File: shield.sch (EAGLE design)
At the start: 36 parts, among them IC1 AD623R, IC2 AD623R, IC3 AD623R

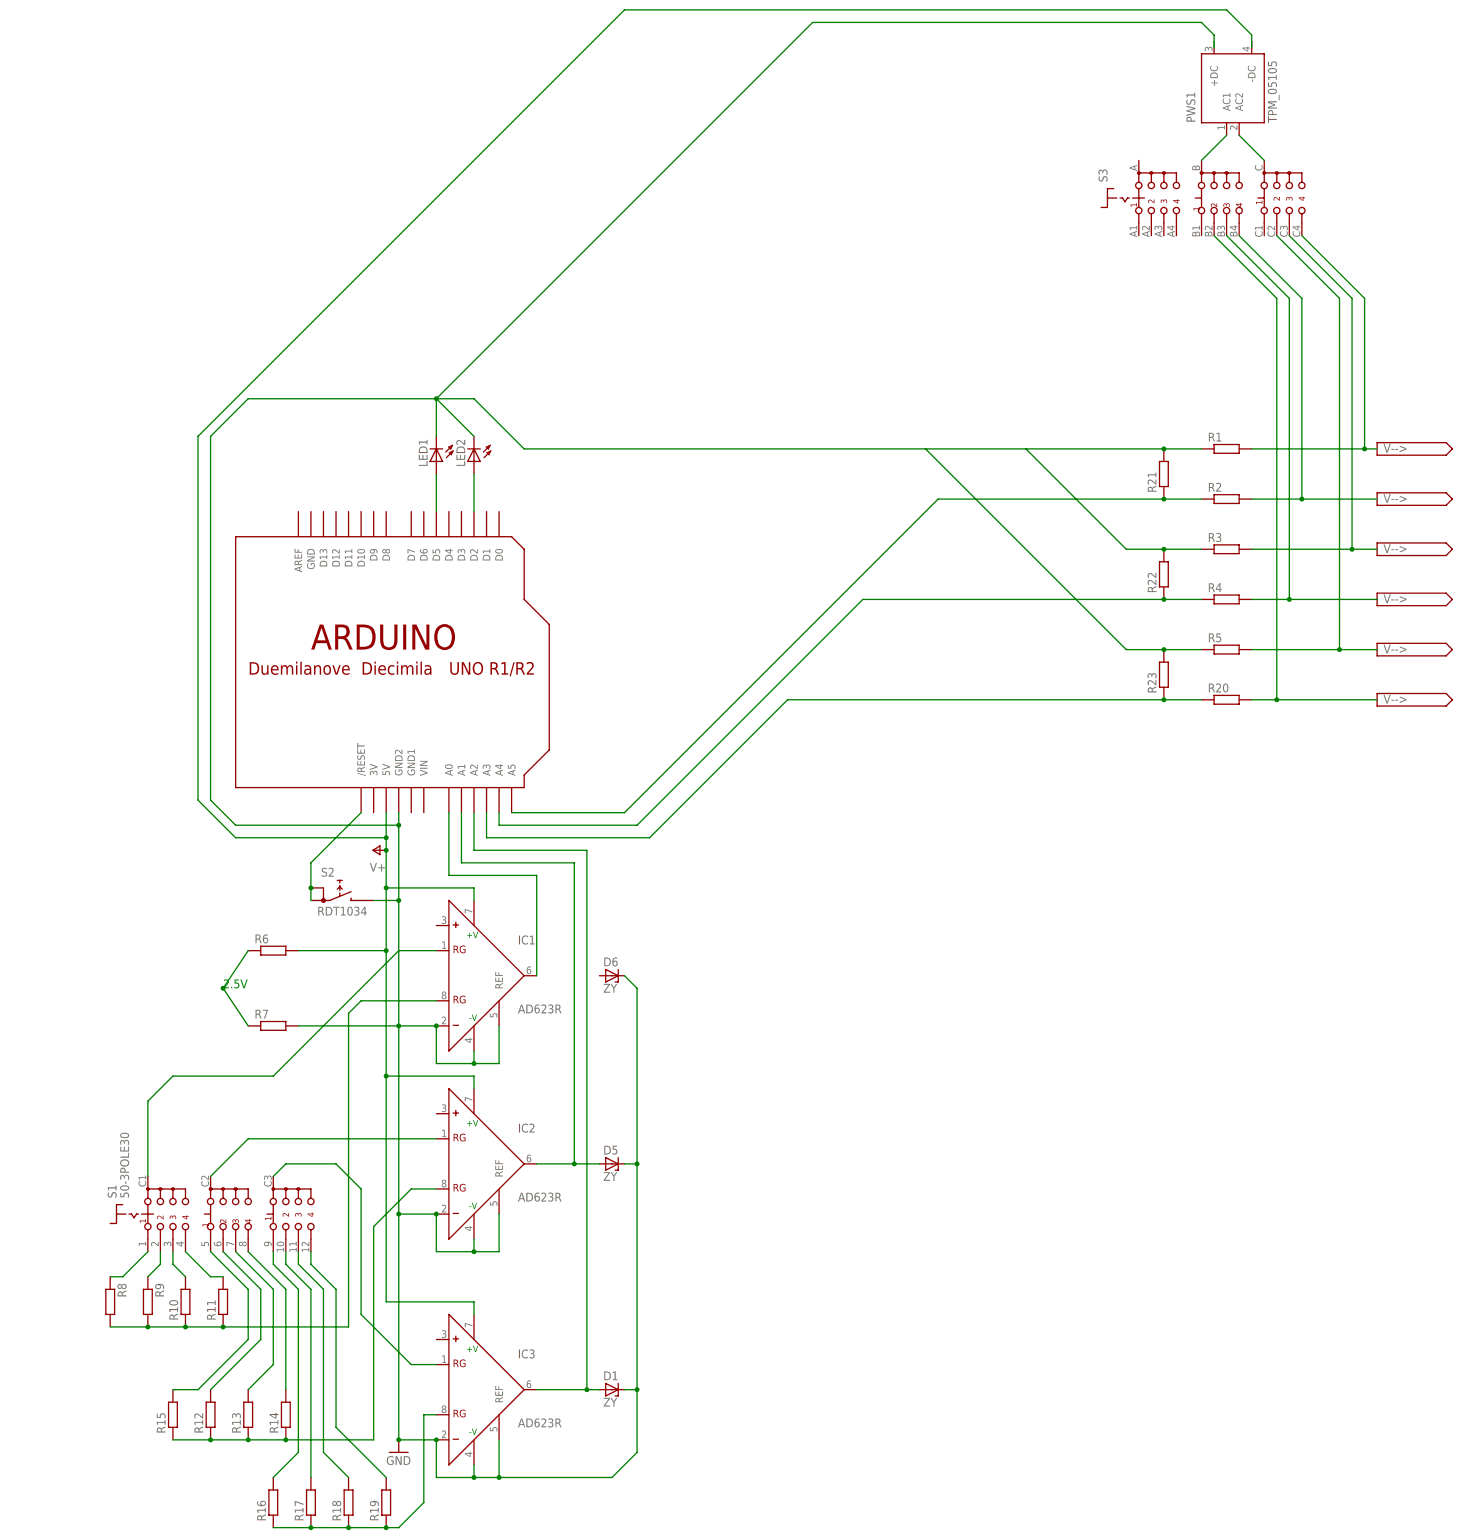
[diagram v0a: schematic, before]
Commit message: Connected A0-A2 amplifiers to signals
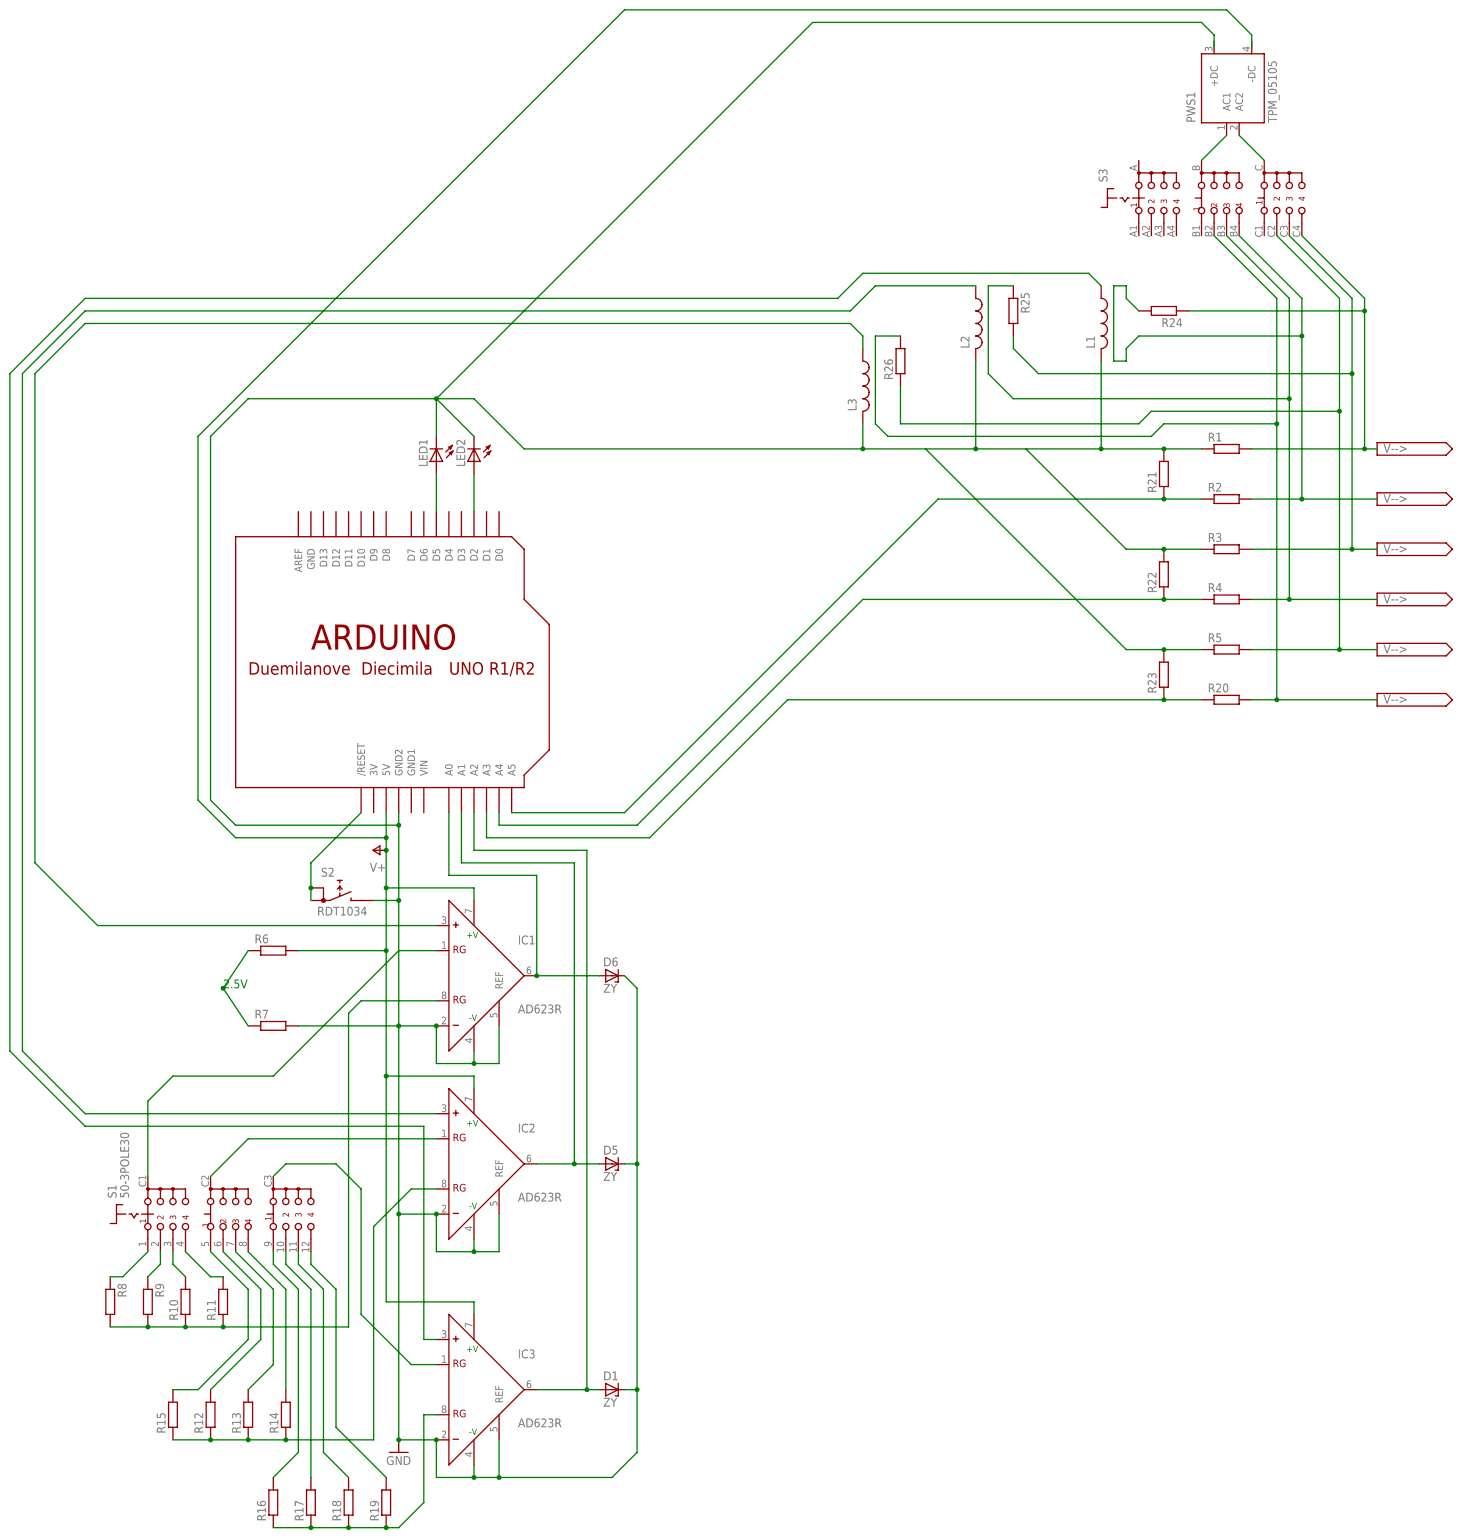
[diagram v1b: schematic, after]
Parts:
- added L1, L2, L3: (no value), resistor:L-USL3216C
- added R24, R25, R26: (no value), resistor:R-EU_0207/10
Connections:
- new net N$38: IC1.+, L3.1
- new net N$40: IC3.+, L1.1
- new net N$42: IC2.+, L2.1
- net GND: now also L1.2, L2.2, L3.2
- net N$10: now also D6.A
- net N$41: now also R24.1
- net N$43: now also R25.2
- net N$45: now also R26.1
- net N$46: now also R26.2
- net N$47: now also R24.2
- net N$48: now also R25.1

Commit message: Fixed some errors
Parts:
- removed R6, R7: (no value), resistor:R-EU_0207/10
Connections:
- removed net N$3: R6.1, R7.1
- removed net N$37: R22.2, R3.1
- removed net N$39: R23.2, R5.1
- net GND: now also R22.2, R23.2, R3.1, R5.1; no longer R7.2
- net V+: no longer R6.2
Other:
- note removed: "2.5V"
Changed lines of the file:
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@@
 <part name="IC3" library="analog-devices" deviceset="AD623" device="R"/>
 <part name="U$1" library="adafruit" deviceset="ARDUINO" device="UNO"/>
-<part name="R6" library="resistor" deviceset="R-EU_" device="0207/10"/>
-<part name="R7" library="resistor" deviceset="R-EU_" device="0207/10"/>
 <part name="S2" library="switch" deviceset="RDT1034" device=""/>
 <part name="S1" library="switch" deviceset="50-3POLE30" device=""/>
@@
 <sheet>
 <plain>
-<text x="-111.76" y="-27.94" size="1.778" layer="91">2.5V</text>
 </plain>
 <instances>
@@
 <instance part="IC3" gate="G$1" x="-60.96" y="-109.22"/>
 <instance part="U$1" gate="G$1" x="-86.36" y="40.64"/>
-<instance part="R6" gate="G$1" x="-101.6" y="-20.32"/>
-<instance part="R7" gate="G$1" x="-101.6" y="-35.56"/>
 <instance part="S2" gate="G$1" x="-88.9" y="-7.62"/>
 <instance part="S1" gate="G$1" x="-114.3" y="-73.66"/>
@@
 </busses>
 <nets>
-<net name="N$3" class="0">
-<segment>
-<pinref part="R6" gate="G$1" pin="1"/>
-<wire x1="-106.68" y1="-20.32" x2="-111.76" y2="-27.94" width="0.1524" layer="91"/>
-<pinref part="R7" gate="G$1" pin="1"/>
-<wire x1="-111.76" y1="-27.94" x2="-106.68" y2="-35.56" width="0.1524" layer="91"/>
-<junction x="-111.76" y="-27.94"/>
-</segment>
-</net>
 <net name="N$4" class="0">
 <segment>
-<pinref part="IC1" gate="G$1" pin="RG@1"/>
-<wire x1="-68.58" y1="-20.32" x2="-76.2" y2="-20.32" width="0.1524" layer="91"/>
-<wire x1="-76.2" y1="-20.32" x2="-101.6" y2="-45.72" width="0.1524" layer="91"/>
-<wire x1="-101.6" y1="-45.72" x2="-121.92" y2="-45.72" width="0.1524" layer="91"/>
-<wire x1="-121.92" y1="-45.72" x2="-127" y2="-50.8" width="0.1524" layer="91"/>
 <pinref part="S1" gate="G$1" pin="A"/>
 <wire x1="-127" y1="-50.8" x2="-127" y2="-66.04" width="0.1524" layer="91"/>
+<pinref part="IC1" gate="G$1" pin="RG@1"/>
+<wire x1="-127" y1="-50.8" x2="-96.52" y2="-20.32" width="0.1524" layer="91"/>
+<wire x1="-96.52" y1="-20.32" x2="-68.58" y2="-20.32" width="0.1524" layer="91"/>
 </segment>
 </net>
@@
 <junction x="-76.2" y="-35.56"/>
 <junction x="-76.2" y="-73.66"/>
-<pinref part="R7" gate="G$1" pin="2"/>
-<wire x1="-96.52" y1="-35.56" x2="-76.2" y2="-35.56" width="0.1524" layer="91"/>
 <pinref part="IC1" gate="G$1" pin="REF"/>
 <wire x1="-55.88" y1="-35.56" x2="-55.88" y2="-43.18" width="0.1524" layer="91"/>
@@
 <wire x1="86.36" y1="81.28" x2="78.74" y2="81.28" width="0.1524" layer="91"/>
 <wire x1="78.74" y1="81.28" x2="66.04" y2="81.28" width="0.1524" layer="91"/>
-<wire x1="66.04" y1="81.28" x2="40.64" y2="81.28" width="0.1524" layer="91"/>
-<wire x1="40.64" y1="81.28" x2="17.78" y2="81.28" width="0.1524" layer="91"/>
+<wire x1="66.04" y1="81.28" x2="50.8" y2="81.28" width="0.1524" layer="91"/>
+<wire x1="50.8" y1="81.28" x2="40.64" y2="81.28" width="0.1524" layer="91"/>
+<wire x1="40.64" y1="81.28" x2="30.48" y2="81.28" width="0.1524" layer="91"/>
+<wire x1="30.48" y1="81.28" x2="17.78" y2="81.28" width="0.1524" layer="91"/>
 <wire x1="17.78" y1="81.28" x2="-50.8" y2="81.28" width="0.1524" layer="91"/>
 <wire x1="-50.8" y1="81.28" x2="-60.96" y2="91.44" width="0.1524" layer="91"/>
@@
 <wire x1="66.04" y1="99.06" x2="66.04" y2="81.28" width="0.1524" layer="91"/>
 <junction x="66.04" y="81.28"/>
+<pinref part="R5" gate="G$1" pin="1"/>
+<pinref part="R23" gate="G$1" pin="2"/>
+<wire x1="86.36" y1="40.64" x2="78.74" y2="40.64" width="0.1524" layer="91"/>
+<wire x1="78.74" y1="40.64" x2="71.12" y2="40.64" width="0.1524" layer="91"/>
+<wire x1="71.12" y1="40.64" x2="30.48" y2="81.28" width="0.1524" layer="91"/>
+<junction x="78.74" y="40.64"/>
+<junction x="30.48" y="81.28"/>
+<pinref part="R3" gate="G$1" pin="1"/>
+<pinref part="R22" gate="G$1" pin="2"/>
+<wire x1="86.36" y1="60.96" x2="78.74" y2="60.96" width="0.1524" layer="91"/>
+<wire x1="78.74" y1="60.96" x2="71.12" y2="60.96" width="0.1524" layer="91"/>
+<wire x1="71.12" y1="60.96" x2="50.8" y2="81.28" width="0.1524" layer="91"/>
+<junction x="78.74" y="60.96"/>
+<junction x="50.8" y="81.28"/>
 </segment>
 </net>
@@
 <segment>
 <pinref part="U$1" gate="G$1" pin="5V"/>
-<junction x="-78.74" y="-20.32"/>
-<wire x1="-78.74" y1="-20.32" x2="-78.74" y2="-45.72" width="0.1524" layer="91"/>
+<wire x1="-78.74" y1="-7.62" x2="-78.74" y2="-45.72" width="0.1524" layer="91"/>
 <wire x1="-78.74" y1="-45.72" x2="-78.74" y2="-91.44" width="0.1524" layer="91"/>
 <wire x1="-78.74" y1="7.62" x2="-78.74" y2="2.54" width="0.1524" layer="91"/>
 <wire x1="-78.74" y1="2.54" x2="-78.74" y2="0" width="0.1524" layer="91"/>
 <wire x1="-78.74" y1="0" x2="-78.74" y2="-7.62" width="0.1524" layer="91"/>
-<wire x1="-78.74" y1="-7.62" x2="-78.74" y2="-20.32" width="0.1524" layer="91"/>
-<wire x1="-78.74" y1="-20.32" x2="-96.52" y2="-20.32" width="0.1524" layer="91"/>
-<pinref part="R6" gate="G$1" pin="2"/>
 <wire x1="-78.74" y1="-91.44" x2="-60.96" y2="-91.44" width="0.1524" layer="91"/>
 <pinref part="IC3" gate="G$1" pin="+V"/>
@@
 </segment>
 </net>
-<net name="N$37" class="0">
-<segment>
-<pinref part="R3" gate="G$1" pin="1"/>
-<pinref part="R22" gate="G$1" pin="2"/>
-<wire x1="86.36" y1="60.96" x2="78.74" y2="60.96" width="0.1524" layer="91"/>
-<wire x1="78.74" y1="60.96" x2="71.12" y2="60.96" width="0.1524" layer="91"/>
-<wire x1="71.12" y1="60.96" x2="50.8" y2="81.28" width="0.1524" layer="91"/>
-<junction x="78.74" y="60.96"/>
-</segment>
-</net>
-<net name="N$39" class="0">
-<segment>
-<pinref part="R5" gate="G$1" pin="1"/>
-<pinref part="R23" gate="G$1" pin="2"/>
-<wire x1="86.36" y1="40.64" x2="78.74" y2="40.64" width="0.1524" layer="91"/>
-<wire x1="78.74" y1="40.64" x2="71.12" y2="40.64" width="0.1524" layer="91"/>
-<wire x1="71.12" y1="40.64" x2="30.48" y2="81.28" width="0.1524" layer="91"/>
-<junction x="78.74" y="40.64"/>
-</segment>
-</net>

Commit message: Fixed more errors
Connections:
- net GND: now also U$1.GND1
- net V+: now also U$1.3V, U$1.VIN
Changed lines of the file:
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@@
 <part name="R25" library="resistor" deviceset="R-EU_" device="0207/10"/>
 <part name="R26" library="resistor" deviceset="R-EU_" device="0207/10"/>
+<part name="P+2" library="supply1" deviceset="V+" device=""/>
+<part name="P+3" library="supply1" deviceset="V+" device=""/>
 </parts>
 <sheets>
@@
 <instance part="IC2" gate="G$1" x="-60.96" y="-63.5"/>
 <instance part="IC3" gate="G$1" x="-60.96" y="-109.22"/>
-<instance part="U$1" gate="G$1" x="-86.36" y="40.64"/>
+<instance part="U$1" gate="G$1" x="-86.36" y="48.26"/>
 <instance part="S2" gate="G$1" x="-88.9" y="-7.62"/>
 <instance part="S1" gate="G$1" x="-114.3" y="-73.66"/>
@@
 <instance part="R25" gate="G$1" x="48.26" y="109.22" rot="R270"/>
 <instance part="R26" gate="G$1" x="25.4" y="99.06" rot="R90"/>
+<instance part="P+2" gate="1" x="-93.98" y="12.7" rot="R90"/>
+<instance part="P+3" gate="1" x="-73.66" y="0" rot="R180"/>
 </instances>
 <busses>
@@
 <segment>
 <pinref part="U$1" gate="G$1" pin="A0"/>
-<wire x1="-66.04" y1="7.62" x2="-66.04" y2="-5.08" width="0.1524" layer="91"/>
+<wire x1="-66.04" y1="15.24" x2="-66.04" y2="-5.08" width="0.1524" layer="91"/>
 <pinref part="IC1" gate="G$1" pin="OUT"/>
 <wire x1="-66.04" y1="-5.08" x2="-48.26" y2="-5.08" width="0.1524" layer="91"/>
@@
 <segment>
 <pinref part="U$1" gate="G$1" pin="A1"/>
-<wire x1="-63.5" y1="7.62" x2="-63.5" y2="-2.54" width="0.1524" layer="91"/>
+<wire x1="-63.5" y1="15.24" x2="-63.5" y2="-2.54" width="0.1524" layer="91"/>
 <wire x1="-63.5" y1="-2.54" x2="-40.64" y2="-2.54" width="0.1524" layer="91"/>
 <wire x1="-40.64" y1="-2.54" x2="-40.64" y2="-63.5" width="0.1524" layer="91"/>
@@
 <segment>
 <pinref part="U$1" gate="G$1" pin="A2"/>
-<wire x1="-60.96" y1="7.62" x2="-60.96" y2="0" width="0.1524" layer="91"/>
+<wire x1="-60.96" y1="15.24" x2="-60.96" y2="0" width="0.1524" layer="91"/>
 <wire x1="-60.96" y1="0" x2="-38.1" y2="0" width="0.1524" layer="91"/>
 <wire x1="-38.1" y1="0" x2="-38.1" y2="-109.22" width="0.1524" layer="91"/>
@@
 <segment>
 <pinref part="U$1" gate="G$1" pin="A3"/>
-<wire x1="-58.42" y1="7.62" x2="-58.42" y2="2.54" width="0.1524" layer="91"/>
+<wire x1="-58.42" y1="15.24" x2="-58.42" y2="2.54" width="0.1524" layer="91"/>
 <wire x1="-58.42" y1="2.54" x2="-25.4" y2="2.54" width="0.1524" layer="91"/>
 <wire x1="-25.4" y1="2.54" x2="2.54" y2="30.48" width="0.1524" layer="91"/>
@@
 <segment>
 <pinref part="U$1" gate="G$1" pin="A4"/>
-<wire x1="-55.88" y1="7.62" x2="-55.88" y2="5.08" width="0.1524" layer="91"/>
+<wire x1="-55.88" y1="15.24" x2="-55.88" y2="5.08" width="0.1524" layer="91"/>
 <wire x1="-55.88" y1="5.08" x2="-27.94" y2="5.08" width="0.1524" layer="91"/>
 <wire x1="-27.94" y1="5.08" x2="17.78" y2="50.8" width="0.1524" layer="91"/>
@@
 <segment>
 <pinref part="U$1" gate="G$1" pin="A5"/>
+<wire x1="-53.34" y1="15.24" x2="-53.34" y2="7.62" width="0.1524" layer="91"/>
 <wire x1="-53.34" y1="7.62" x2="-30.48" y2="7.62" width="0.1524" layer="91"/>
 <wire x1="-30.48" y1="7.62" x2="33.02" y2="71.12" width="0.1524" layer="91"/>
@@
 <net name="N$19" class="0">
 <segment>
-<pinref part="U$1" gate="G$1" pin="/RESET"/>
-<wire x1="-83.82" y1="7.62" x2="-93.98" y2="-2.54" width="0.1524" layer="91"/>
 <pinref part="S2" gate="G$1" pin="A1"/>
 <wire x1="-93.98" y1="-2.54" x2="-93.98" y2="-7.62" width="0.1524" layer="91"/>
@@
 <wire x1="-93.98" y1="-7.62" x2="-93.98" y2="-10.16" width="0.1524" layer="91"/>
 <junction x="-93.98" y="-7.62"/>
+<pinref part="U$1" gate="G$1" pin="/RESET"/>
+<wire x1="-83.82" y1="15.24" x2="-83.82" y2="7.62" width="0.1524" layer="91"/>
+<wire x1="-83.82" y1="7.62" x2="-93.98" y2="-2.54" width="0.1524" layer="91"/>
 </segment>
 </net>
@@
 <pinref part="LED2" gate="G$1" pin="A"/>
 <pinref part="U$1" gate="G$1" pin="D2"/>
-<wire x1="-60.96" y1="76.2" x2="-60.96" y2="68.58" width="0.1524" layer="91"/>
 </segment>
 </net>
@@
 <pinref part="LED1" gate="G$1" pin="A"/>
 <pinref part="U$1" gate="G$1" pin="D5"/>
-<wire x1="-68.58" y1="76.2" x2="-68.58" y2="68.58" width="0.1524" layer="91"/>
 </segment>
 </net>
@@
 <junction x="-60.96" y="-127"/>
 <pinref part="U$1" gate="G$1" pin="GND2"/>
-<wire x1="-76.2" y1="7.62" x2="-76.2" y2="5.08" width="0.1524" layer="91"/>
+<wire x1="-76.2" y1="15.24" x2="-76.2" y2="5.08" width="0.1524" layer="91"/>
 <pinref part="S2" gate="G$1" pin="B"/>
 <wire x1="-76.2" y1="5.08" x2="-76.2" y2="-10.16" width="0.1524" layer="91"/>
@@
 <junction x="78.74" y="60.96"/>
 <junction x="50.8" y="81.28"/>
+<pinref part="U$1" gate="G$1" pin="GND1"/>
+<wire x1="-73.66" y1="15.24" x2="-73.66" y2="7.62" width="0.1524" layer="91"/>
+<wire x1="-73.66" y1="7.62" x2="-76.2" y2="5.08" width="0.1524" layer="91"/>
 </segment>
 </net>
@@
 <wire x1="-78.74" y1="-7.62" x2="-78.74" y2="-45.72" width="0.1524" layer="91"/>
 <wire x1="-78.74" y1="-45.72" x2="-78.74" y2="-91.44" width="0.1524" layer="91"/>
-<wire x1="-78.74" y1="7.62" x2="-78.74" y2="2.54" width="0.1524" layer="91"/>
+<wire x1="-78.74" y1="15.24" x2="-78.74" y2="2.54" width="0.1524" layer="91"/>
 <wire x1="-78.74" y1="2.54" x2="-78.74" y2="0" width="0.1524" layer="91"/>
 <wire x1="-78.74" y1="0" x2="-78.74" y2="-7.62" width="0.1524" layer="91"/>
@@
 <wire x1="-30.48" y1="170.18" x2="-116.84" y2="83.82" width="0.1524" layer="91"/>
 </segment>
-</net>
+<segment>
+<pinref part="U$1" gate="G$1" pin="3V"/>
+<pinref part="P+2" gate="1" pin="V+"/>
+<wire x1="-81.28" y1="15.24" x2="-81.28" y2="12.7" width="0.1524" layer="91"/>
+<wire x1="-81.28" y1="12.7" x2="-91.44" y2="12.7" width="0.1524" layer="91"/>
+</segment>
+<segment>
+<pinref part="P+3" gate="1" pin="V+"/>
+<pinref part="U$1" gate="G$1" pin="VIN"/>
+<wire x1="-73.66" y1="2.54" x2="-71.12" y2="5.08" width="0.1524" layer="91"/>
+<wire x1="-71.12" y1="5.08" x2="-71.12" y2="15.24" width="0.1524" layer="91"/>
+</segment>
+</net>
